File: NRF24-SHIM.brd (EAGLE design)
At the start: 27.9 x 50.8 mm, 15 parts, among them M1 WIRELESS-NRF24L01, M2 WIRELESS-NRF24L01-PA-EXT

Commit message: removed some unneeded stuff from the board.
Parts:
- moved LOGO2 1.27 mm to (1.02, -4.57)
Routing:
- net GND: track 2.17 -> 0.00 mm, vias 47 -> 42
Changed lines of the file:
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@@
 <text x="16.256" y="25.654" size="1.016" layer="22" font="vector" ratio="12" rot="MR180">SPI0</text>
 <text x="16.256" y="34.29" size="1.016" layer="22" font="vector" ratio="12" rot="MR180">SPI1</text>
-<text x="20.066" y="22.352" size="1.016" layer="22" font="vector" ratio="12" rot="MR0">SPI bus selection</text>
+<text x="20.32" y="22.86" size="1.016" layer="22" font="vector" ratio="12" rot="MR0">SPI bus selection</text>
 <rectangle x1="0" y1="48.26" x2="2.54" y2="50.8" layer="21"/>
 <rectangle x1="22.86" y1="48.26" x2="25.4" y2="50.8" layer="21"/>
-<circle x="6.604" y="31.369" radius="0.127" width="0.2032" layer="21"/>
 <text x="14.351" y="3.302" size="1.016" layer="21" font="vector" ratio="12">-</text>
 <text x="20.32" y="35.56" size="1.016" layer="22" font="vector" ratio="12" rot="MR0">(c) Andriy Golovnya</text>
@@
 </element>
 <element name="LOGO1" library="_my_logos" package="MFDEC_SQ_8MM" value="MFDECLOGO_SQ_8MM" x="8.89" y="39.37" smashed="yes"/>
-<element name="LOGO2" library="_my_logos" package="MFDEC_L_20MM" value="MFDECLOGO_L_20MM" x="-0.254" y="-4.572" smashed="yes" rot="MR90"/>
+<element name="LOGO2" library="_my_logos" package="MFDEC_L_20MM" value="MFDECLOGO_L_20MM" x="1.016" y="-4.572" smashed="yes" rot="MR90"/>
 <element name="LOGO3" library="_my_logos" package="RSNURL_QR_10MM" value="RSNURL_QR_10MM" x="19.05" y="39.37" smashed="yes" rot="MR0"/>
 <element name="M1" library="diy-modules" package="WIRELESS-NRF24L01" value="WIRELESS-NRF24L01" x="15.24" y="15.24" smashed="yes" rot="R90">
-<attribute name="NAME" x="21.59" y="1.905" size="0.6096" layer="25" font="vector" rot="R90"/>
-<attribute name="VALUE" x="21.59" y="3.937" size="0.6096" layer="27" font="vector" rot="R90"/>
+<attribute name="NAME" x="21.59" y="1.397" size="0.6096" layer="25" font="vector" rot="R90"/>
+<attribute name="VALUE" x="21.59" y="3.81" size="0.6096" layer="27" font="vector" rot="R90"/>
 </element>
 <element name="M2" library="diy-modules" package="WIRELESS-NRF24L01-PA-EXT" value="WIRELESS-NRF24L01-PA-EXT" x="12.7" y="20.955" smashed="yes" rot="R90">
-<attribute name="NAME" x="6.477" y="1.778" size="0.6096" layer="25" font="vector" rot="R90"/>
-<attribute name="VALUE" x="6.477" y="3.937" size="0.6096" layer="27" font="vector" rot="R90"/>
+<attribute name="NAME" x="6.35" y="1.27" size="0.6096" layer="25" font="vector" rot="R90"/>
+<attribute name="VALUE" x="6.223" y="3.81" size="0.6096" layer="27" font="vector" rot="R90"/>
 </element>
 </elements>
@@
 <vertex x="33.147" y="0"/>
 </polygon>
-<via x="19.304" y="49.403" extent="1-16" drill="0.35"/>
-<via x="6.223" y="49.403" extent="1-16" drill="0.35"/>
-<via x="12.446" y="49.657" extent="1-16" drill="0.35"/>
-<via x="12.446" y="47.117" extent="1-16" drill="0.35"/>
-<via x="4.826" y="25.527" extent="1-16" drill="0.35"/>
-<via x="4.826" y="20.447" extent="1-16" drill="0.35"/>
-<via x="4.826" y="17.653" extent="1-16" drill="0.35"/>
+<via x="22.098" y="49.53" extent="1-16" drill="0.35"/>
+<via x="6.223" y="49.53" extent="1-16" drill="0.35"/>
+<via x="14.478" y="49.657" extent="1-16" drill="0.35"/>
+<via x="14.478" y="47.117" extent="1-16" drill="0.35"/>
 <via x="5.588" y="1.016" extent="1-16" drill="0.35"/>
-<via x="19.558" y="1.143" extent="1-16" drill="0.35"/>
-<via x="19.558" y="25.527" extent="1-16" drill="0.35"/>
-<via x="4.826" y="30.607" extent="1-16" drill="0.35"/>
+<via x="21.717" y="0.762" extent="1-16" drill="0.35"/>
 <via x="25.4" y="7.62" extent="1-16" drill="0.35"/>
 <via x="25.4" y="12.7" extent="1-16" drill="0.35"/>
@@
 <via x="2.54" y="35.56" extent="1-16" drill="0.35"/>
 <via x="2.54" y="38.1" extent="1-16" drill="0.35"/>
-<wire x1="2.667" y1="28.067" x2="2.8194" y2="27.9146" width="0.254" layer="16"/>
-<wire x1="2.8194" y1="27.9146" x2="4.7752" y2="27.9146" width="0.254" layer="16"/>
 <via x="25.4" y="27.94" extent="1-16" drill="0.35"/>
 <contactref element="M1" pad="1"/>
@@
 <wire x1="25.4" y1="2.54" x2="25.4" y2="5.08" width="0" layer="19" extent="1-1"/>
 <wire x1="24.003" y1="1.27" x2="25.4" y2="2.54" width="0" layer="19" extent="1-1"/>
-<wire x1="19.558" y1="1.143" x2="24.003" y2="1.27" width="0" layer="19" extent="1-1"/>
-<wire x1="19.558" y1="25.527" x2="25.4" y2="25.4" width="0" layer="19" extent="1-1"/>
-<wire x1="19.304" y1="49.403" x2="25.4" y2="48.26" width="0" layer="19" extent="1-1"/>
-<wire x1="12.446" y1="49.657" x2="19.304" y2="49.403" width="0" layer="19" extent="1-1"/>
-<wire x1="12.446" y1="47.117" x2="12.446" y2="49.657" width="0" layer="19" extent="1-1"/>
-<wire x1="6.223" y1="49.403" x2="12.446" y2="49.657" width="0" layer="19" extent="1-1"/>
-<wire x1="2.54" y1="45.72" x2="6.223" y2="49.403" width="0" layer="19" extent="1-1"/>
+<wire x1="21.717" y1="0.762" x2="24.003" y2="1.27" width="0" layer="19" extent="1-1"/>
+<wire x1="22.098" y1="49.53" x2="25.4" y2="48.26" width="0" layer="19" extent="1-1"/>
+<wire x1="14.478" y1="49.657" x2="22.098" y2="49.53" width="0" layer="19" extent="1-1"/>
+<wire x1="14.478" y1="47.117" x2="14.478" y2="49.657" width="0" layer="19" extent="1-1"/>
+<wire x1="6.223" y1="49.53" x2="14.478" y2="49.657" width="0" layer="19" extent="1-1"/>
+<wire x1="2.54" y1="45.72" x2="6.223" y2="49.53" width="0" layer="19" extent="1-1"/>
 <wire x1="3.937" y1="44.45" x2="2.54" y2="45.72" width="0" layer="19" extent="1-1"/>
 <wire x1="2.54" y1="43.18" x2="3.937" y2="44.45" width="0" layer="19" extent="1-1"/>
@@
 <wire x1="2.54" y1="33.02" x2="3.937" y2="34.29" width="0" layer="19" extent="1-1"/>
 <wire x1="2.54" y1="30.48" x2="2.54" y2="33.02" width="0" layer="19" extent="1-1"/>
-<wire x1="4.826" y1="30.607" x2="2.54" y2="30.48" width="0" layer="19" extent="1-1"/>
-<wire x1="2.667" y1="28.067" x2="2.54" y2="30.48" width="0" layer="19" extent="16-16"/>
-<wire x1="3.683" y1="26.67" x2="4.7752" y2="27.9146" width="0" layer="19" extent="16-16"/>
-<wire x1="4.826" y1="25.527" x2="3.683" y2="26.67" width="0" layer="19" extent="1-1"/>
+<wire x1="3.683" y1="26.67" x2="2.54" y2="30.48" width="0" layer="19" extent="1-1"/>
 <wire x1="2.54" y1="25.4" x2="3.683" y2="26.67" width="0" layer="19" extent="1-1"/>
 <wire x1="2.54" y1="22.86" x2="2.54" y2="25.4" width="0" layer="19" extent="1-1"/>
@@
 <wire x1="1.397" y1="19.05" x2="2.54" y2="20.32" width="0" layer="19" extent="1-1"/>
 <wire x1="2.54" y1="17.78" x2="1.397" y2="19.05" width="0" layer="19" extent="1-1"/>
-<wire x1="4.826" y1="20.447" x2="2.54" y2="20.32" width="0" layer="19" extent="1-1"/>
-<wire x1="4.826" y1="17.653" x2="2.54" y2="17.78" width="0" layer="19" extent="1-1"/>
 <wire x1="2.54" y1="15.24" x2="2.54" y2="17.78" width="0" layer="19" extent="1-1"/>
 <wire x1="3.937" y1="13.97" x2="2.54" y2="15.24" width="0" layer="19" extent="1-1"/>

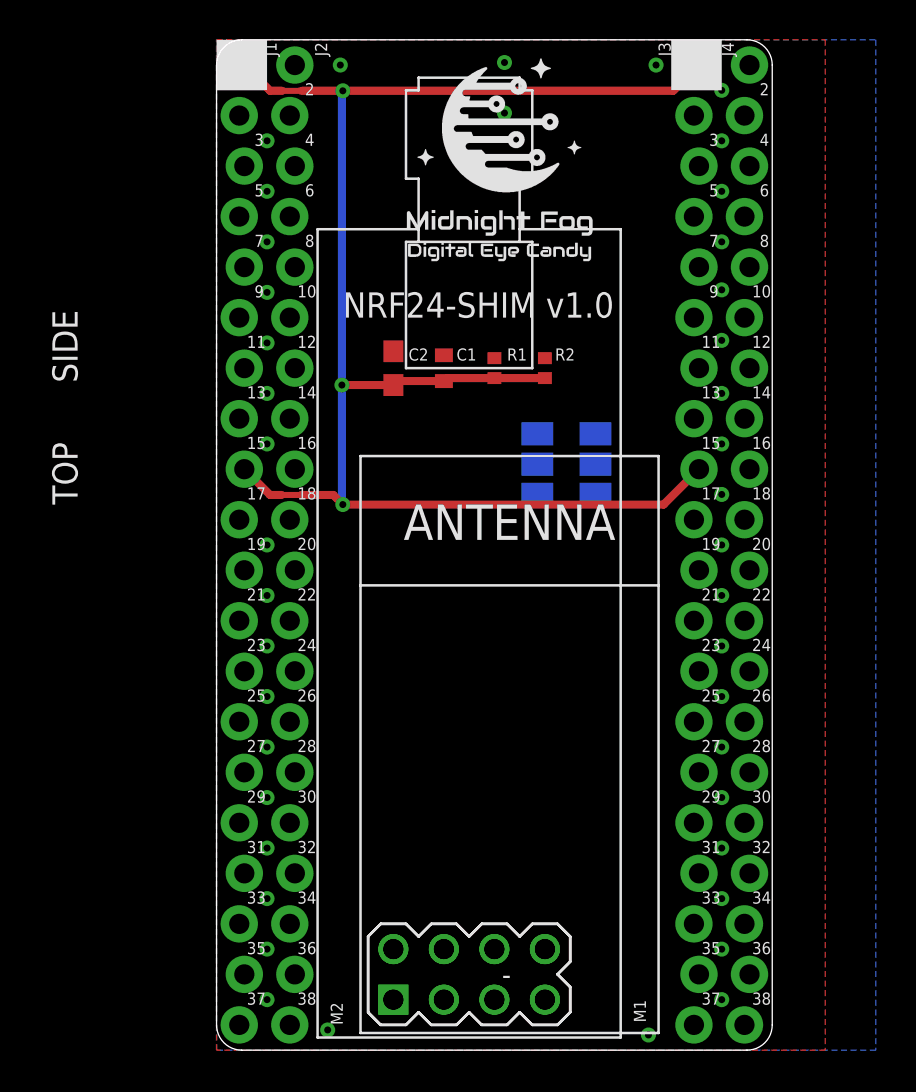
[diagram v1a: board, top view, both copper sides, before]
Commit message: Add more pullups. Add more solder joints. Did some tracing.
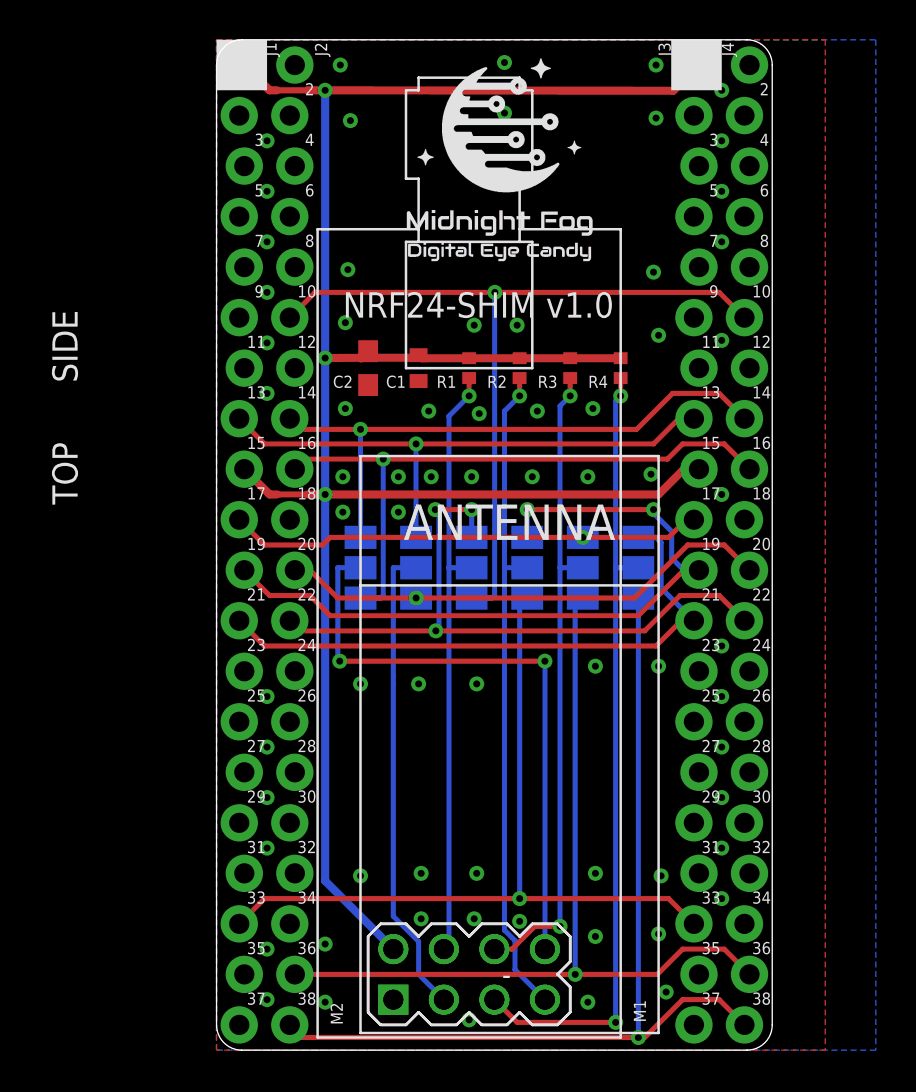
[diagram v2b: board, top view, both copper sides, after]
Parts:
- added R3, R4: 10K, rcl:R0402
- added SJ3, SJ4, SJ5, SJ6: (no value), _my_jumpers:SJ_2
- moved SJ1 7.27 mm to (21.2, 24.3)
- moved SJ2 5.25 mm to (18.4, 24.3)
- moved R1 1.27 mm to (12.7, 34.3), turned to 90 degrees
- moved R2 1.27 mm to (15.2, 34.3), turned to 90 degrees
- moved C2 1.27 mm to (7.62, 34.3), turned to 270 degrees
- moved C1 1.27 mm to (10.2, 34.3), turned to 270 degrees
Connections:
- removed net VCC: M1.2, M2.2
- new net CE: M1.3, M2.3, SJ5.2
- new net CE0: J1.8, J3.8, SJ5.1
- new net CE1: J2.11, J4.11, SJ5.3
- new net CSN: M1.4, M2.4, R1.1, SJ4.2
- new net CSN0: J2.12, J4.12, SJ4.1
- new net CSN1: J2.6, J4.6, SJ4.3
- new net IRQ: M1.8, M2.8, SJ6.2
- new net IRQ0: J2.8, J4.8, SJ6.1
- new net IRQ1: J2.9, J4.9, SJ6.3
- new net MISO: M1.7, M2.7, R2.1, SJ3.2
- new net MISO0: J1.11, J3.11, SJ3.1
- new net MISO1: J1.18, J3.18, SJ3.3
- new net MOSI: M1.6, M2.6, R3.1, SJ2.2
- new net MOSI0: J1.10, J3.10, SJ2.1
- new net MOSI1: J2.19, J4.19, SJ2.3
- new net SCK: M1.5, M2.5, R4.1, SJ1.2
- new net SCK0: J1.12, J3.12, SJ1.1
- new net SCK1: J2.20, J4.20, SJ1.3
- net 3.3V: now also M1.2, M2.2, R3.2, R4.2
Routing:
- net SCK1: track 0.00 -> 46.5 mm, vias 0 -> 1
- net MOSI1: track 0.00 -> 43.0 mm, vias 0 -> 1
- net CSN1: track 0.00 -> 40.4 mm, vias 0 -> 1
- net SCK: track 0.00 -> 40.2 mm, vias 0 -> 2
- net MISO1: track 0.00 -> 39.2 mm, vias 0 -> 1
- net MISO0: track 0.00 -> 36.9 mm, vias 0 -> 2
- net CSN0: track 0.00 -> 33.8 mm, vias 0 -> 3
- net MISO: track 0.00 -> 33.6 mm, vias 0 -> 1
- net MOSI: track 0.00 -> 32.7 mm, vias 0 -> 2
- net IRQ1: track 0.00 -> 32.0 mm, vias 0 -> 1
- net IRQ: track 0.00 -> 30.7 mm, vias 0 -> 2
- net CSN: track 0.00 -> 30.4 mm, vias 0 -> 1
- net IRQ0: track 0.00 -> 29.8 mm, vias 0 -> 1
- net SCK0: track 0.00 -> 29.8 mm
- net CE0: track 0.00 -> 28.6 mm, vias 0 -> 1
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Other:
- board text removed: "SPI0"
- board text removed: "SPI1"

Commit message: Changed NRF24 connector to locked one. Moved passive components closer to the NRF24 connector. Add descriptive texts. Moved some stuff around.
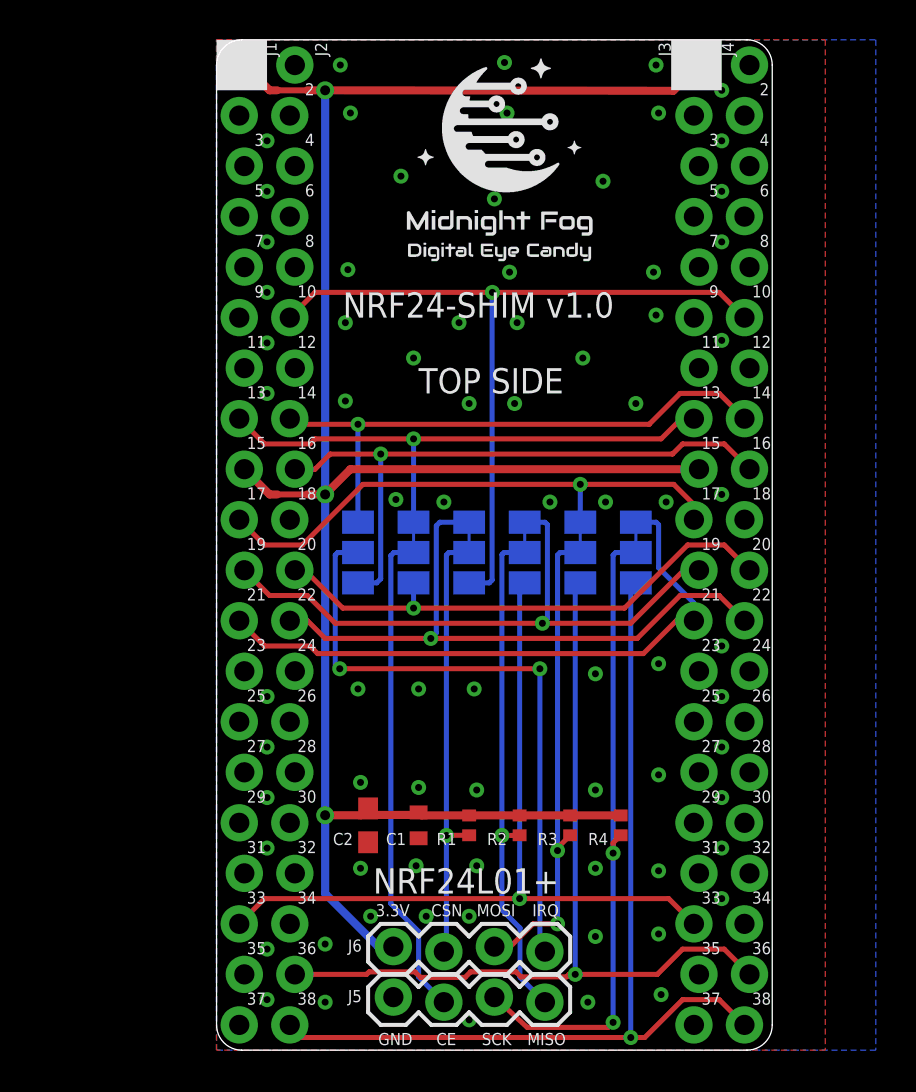
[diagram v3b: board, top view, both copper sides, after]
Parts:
- removed M1: WIRELESS-NRF24L01, diy-modules:WIRELESS-NRF24L01
- removed M2: WIRELESS-NRF24L01-PA-EXT, diy-modules:WIRELESS-NRF24L01-PA-EXT
- added J5, J6: (no value), SparkFun-Connectors:1X04_LOCK
- moved C1 23.0 mm to (10.2, 11.3)
- moved C2 23.0 mm to (7.62, 11.3)
- moved R1 23.0 mm to (12.7, 11.3)
- moved R2 23.0 mm to (15.2, 11.3)
- moved R3 23.0 mm to (17.8, 11.3)
- moved R4 23.0 mm to (20.3, 11.3)
- moved SJ3 0.77 mm to (15.5, 25.0)
- moved SJ4 0.77 mm to (12.7, 25.0)
- moved SJ6 0.77 mm to (7.11, 25.0)
- moved SJ1 0.77 mm to (21.1, 25.0)
- moved SJ2 0.77 mm to (18.3, 25.0)
- moved SJ5 0.77 mm to (9.91, 25.0)
- moved LOGO2 0.57 mm to (1.27, -5.08)
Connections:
- net 3.3V: now also J6.1; no longer M1.2, M2.2
- net CE: now also J5.2; no longer M1.3, M2.3
- net CSN: now also J6.2; no longer M1.4, M2.4
- net GND: now also J5.1; no longer M1.1, M2.1
- net IRQ: now also J6.4; no longer M1.8, M2.8
- net MISO: now also J5.4; no longer M1.7, M2.7
- net MOSI: now also J6.3; no longer M1.6, M2.6
- net SCK: now also J5.3; no longer M1.5, M2.5
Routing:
- net MOSI: track 32.7 -> 25.6 mm
- net MISO: track 33.6 -> 26.7 mm
- net CSN: track 30.4 -> 23.6 mm
- net SCK: track 40.2 -> 33.6 mm
- net MISO0: track 36.9 -> 31.3 mm, vias 2 -> 1
- net MOSI0: track 23.9 -> 27.7 mm
- net CE: track 23.9 -> 26.0 mm
- net CE1: track 25.1 -> 26.8 mm
- net CSN0: track 33.8 -> 32.2 mm, vias 3 -> 1
- net SCK0: track 29.8 -> 31.0 mm
- net MOSI1: track 43.0 -> 44.1 mm
- net SCK1: track 46.5 -> 47.4 mm
- net IRQ: track 30.7 -> 31.5 mm
- net CSN1: track 40.4 -> 39.6 mm
- net IRQ0: track 29.8 -> 29.1 mm
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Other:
- board text added: "3.3V"
- board text added: "CE"
- board text added: "CSN"
- board text added: "CSN0"
- board text added: "CSN1"
- board text added: "GND"
- board text added: "IO22"
- board text added: "IO23"
- board text added: "IO24"
- board text added: "IO25"
- board text added: "IRQ"
- board text added: "MISO"
- board text added: "MISO0"
- board text added: "MISO1"
- board text added: "MOSI"
- board text added: "MOSI0"
- board text added: "MOSI1"
- board text added: "NRF24L01+"
- board text added: "SCK"
- board text added: "SCK0"
- board text added: "SCK1"
- board text added: "SPI bus select. CE IRQ"
- board text removed: "SPI bus selection"
